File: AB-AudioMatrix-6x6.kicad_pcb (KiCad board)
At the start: 2 copper layers, 204 x 103 mm, 53 parts, among them J1 AudioJack2_Ground_Switch, J10 AudioJack2_Ground_Switch, J11 AudioJack2_Ground_Switch, J12 AudioJack2_Ground_Switch, J13 Conn_01x24, J14 Conn_01x24, J15 Screw_Terminal_01x03, J16 Conn_01x24, J17 Conn_01x24, J2 AudioJack2_Ground_Switch, J3 AudioJack2_Ground_Switch, J4 AudioJack2_Ground_Switch, J5 AudioJack2_Ground_Switch, J6 AudioJack2_Ground_Switch, J7 AudioJack2_Ground_Switch, J8 AudioJack2_Ground_Switch, J9 AudioJack2_Ground_Switch, SW1 SW_Rotary2x6, SW2 SW_Rotary2x6, SW3 SW_Rotary2x6, SW4 SW_Rotary2x6, SW5 SW_Rotary2x6, SW6 SW_Rotary2x6, U1 TL072, U2 TL072, U3 TL072, U4 TL072, U5 TL072, U6 TL072

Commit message: added Edge.Cuts | devices arranged on PCB | added GND planes
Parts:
- added ?: Symbol_CreativeCommonsPublicDomain_SilkScreenTop_Small, Symbol:Symbol_CreativeCommonsPublicDomain_SilkScreenTop_Small, F.Cu at (97.0, 154.9)
- added REF**: KiCad-Logo2_6mm_SilkScreen, Symbol:KiCad-Logo2_6mm_SilkScreen, F.Cu at (51.0, 154.7)
- added REF**: MountingHole_3.2mm_M3, MountingHole:MountingHole_3.2mm_M3, F.Cu at (47.0, 100.0)
- added REF**: MountingHole_3.2mm_M3, MountingHole:MountingHole_3.2mm_M3, F.Cu at (138.0, 100.0)
- added REF**: MountingHole_3.2mm_M3, MountingHole:MountingHole_3.2mm_M3, F.Cu at (148.0, 100.0)
- added REF**: MountingHole_3.2mm_M3, MountingHole:MountingHole_3.2mm_M3, F.Cu at (239.0, 100.0)
- added REF**: MountingHole_3.2mm_M3, MountingHole:MountingHole_3.2mm_M3, F.Cu at (113.0, 110.0)
- added REF**: MountingHole_3.2mm_M3, MountingHole:MountingHole_3.2mm_M3, F.Cu at (173.0, 110.0)
- added REF**: OSHW-Logo2_9.8x8mm_SilkScreen, Symbol:OSHW-Logo2_9.8x8mm_SilkScreen, F.Cu at (64.0, 154.0)
- added REF**: Symbol_CC-Attribution_CopperTop_Small, Symbol:Symbol_CC-Attribution_CopperTop_Small, F.Cu at (72.0, 155.0)
- added REF**: MountingHole_3.2mm_M3, MountingHole:MountingHole_3.2mm_M3, F.Cu at (47.0, 144.0)
- added REF**: MountingHole_3.2mm_M3, MountingHole:MountingHole_3.2mm_M3, F.Cu at (113.0, 144.0)
- added REF**: MountingHole_3.2mm_M3, MountingHole:MountingHole_3.2mm_M3, F.Cu at (173.0, 144.0)
- added REF**: MountingHole_3.2mm_M3, MountingHole:MountingHole_3.2mm_M3, F.Cu at (239.0, 144.0)
- added REF**: MountingHole_3.2mm_M3, MountingHole:MountingHole_3.2mm_M3, F.Cu at (239.0, 110.0)
- added REF**: MountingHole_3.2mm_M3, MountingHole:MountingHole_3.2mm_M3, F.Cu at (47.0, 110.0)
- J1, J10, J11, J12, J2, J3, J4, J5, J6, J7, J8, J9: value AudioJack2_Ground_Switch -> Switchcraft-35RAPC4BH3
- J13, J14, J16, J17, R1, R10, R11, R12, R13, R14, R15, R16, R17, R18, R19, R2, R20, R21, R22, R23, R24, R3, R4, R5, R6, R7, R8, R9, U1, U2, U3, U4, U5, U6: moved to B.Cu
- moved R18 234.1 mm to (230.1, 83.0)
- moved R24 230.7 mm to (237.1, 83.0)
- moved R23 215.0 mm to (221.7, 83.0)
- moved R21 211.4 mm to (190.9, 83.0)
- moved R17 209.7 mm to (214.7, 83.0)
- moved R16 207.2 mm to (199.3, 83.0)
- moved R14 202.5 mm to (168.5, 83.0)
- moved R22 201.0 mm to (206.3, 83.0)
- moved R20 199.7 mm to (175.5, 83.0)
- moved R15 195.7 mm to (183.9, 83.0)
- moved R13 182.3 mm to (153.1, 83.0)
- moved R12 181.8 mm to (129.1, 83.0), turned to 90 degrees
- moved R19 180.1 mm to (160.1, 83.0)
- moved R5 179.3 mm to (120.7, 83.0), turned to 90 degrees
- moved R8 178.3 mm to (67.5, 83.0), turned to 90 degrees
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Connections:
- J15 pad 1: +9V -> -9V
- J15 pad 3: -9V -> +9V
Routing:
- added copper zone on In1.Cu, net GND
- added copper zone on In2.Cu, net GND
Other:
- board size 204 x 103 mm -> 200 x 70 mm
- copper layers 2 -> 4
- board text added: "+"
- board text added: "—"

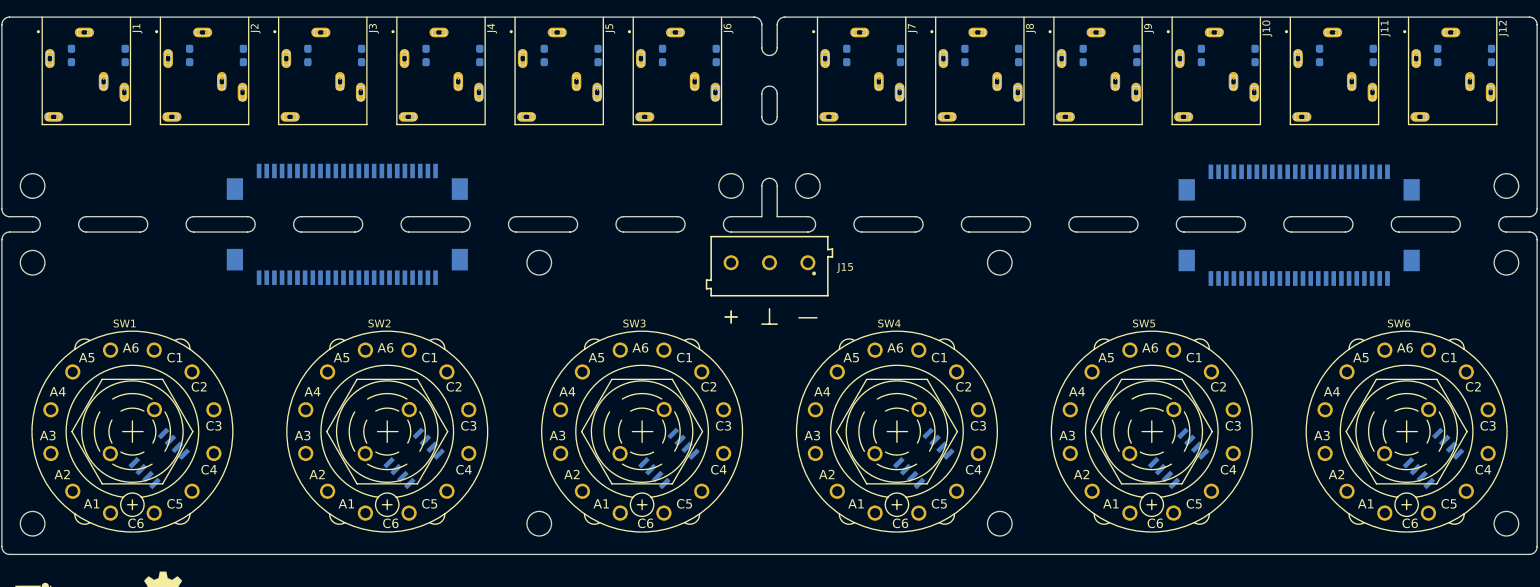
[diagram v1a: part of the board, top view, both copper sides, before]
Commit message: added converter for asymmetric power supply | Routing In & Out PCB finished | Routing Switch PCB started
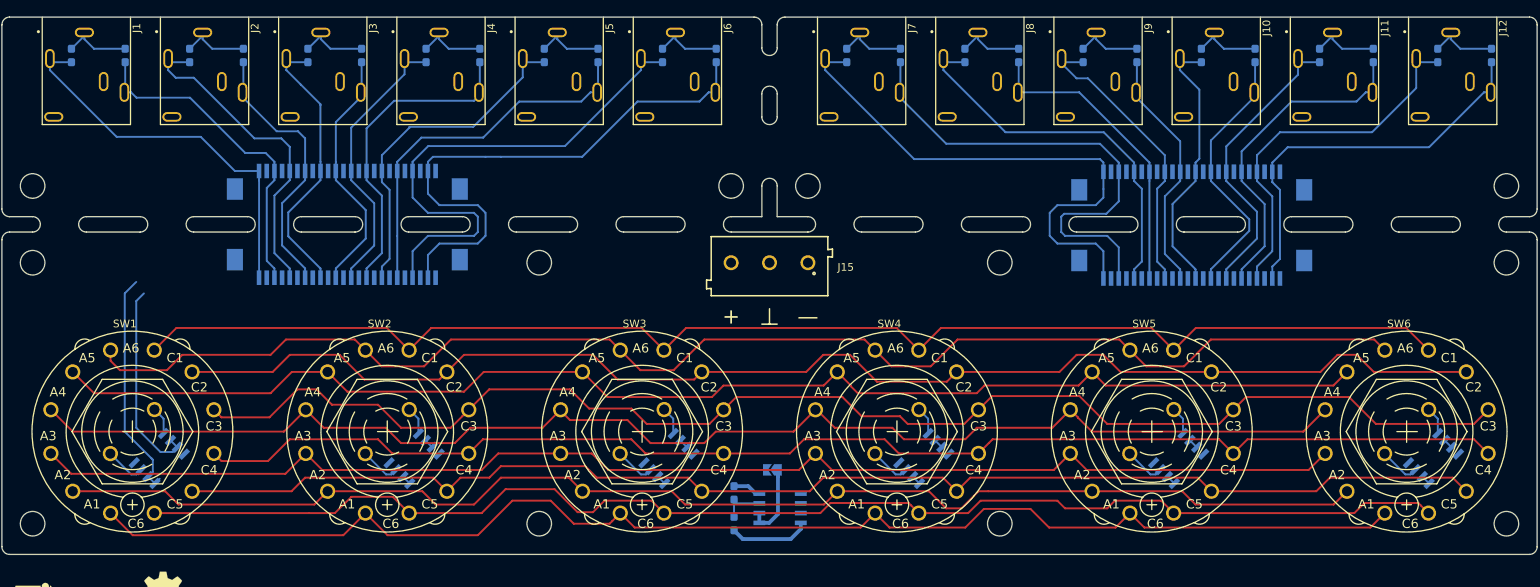
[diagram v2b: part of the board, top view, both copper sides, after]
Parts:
- added JP1: SolderJumper_2_Open, Jumper:SolderJumper-2_P1.3mm_Open_TrianglePad1.0x1.5mm, B.Cu at (143.4, 137.0)
- added R25: 100k, Resistor_SMD:R_0603_1608Metric_Pad1.05x0.95mm_HandSolder, B.Cu at (138.4, 144.0)
- added R26: 100k, Resistor_SMD:R_0603_1608Metric_Pad1.05x0.95mm_HandSolder, B.Cu at (138.4, 140.0)
- added U7: TL072, Package_SO:SOIC-8_3.9x4.9mm_P1.27mm, B.Cu at (144.4, 142.0)
- moved J16 14.0 mm to (198.0, 109.1)
- moved J17 14.0 mm to (198.0, 101.1)
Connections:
- J13 pad 1: In1R -> In1L
- J13 pad 11: In3L -> In3R
- J13 pad 13: In4R -> In4L
- J13 pad 15: In4L -> In4R
- J13 pad 17: In5R -> In5L
- J13 pad 19: In5L -> In5R
- J13 pad 21: In6R -> In6L
- J13 pad 23: In6L -> In6R
- J13 pad 3: In1L -> In1R
- J13 pad 5: In2R -> In2L
- J13 pad 7: In2L -> In2R
- J13 pad 9: In3R -> In3L
- J14 pad 10: In4L -> In4R
- J14 pad 12: In4R -> In4L
- J14 pad 14: In3L -> In3R
- J14 pad 16: In3R -> In3L
- J14 pad 18: In2L -> In2R
- J14 pad 2: In6L -> In6R
- J14 pad 20: In2R -> In2L
- J14 pad 22: In1L -> In1R
- J14 pad 24: In1R -> In1L
- J14 pad 4: In6R -> In6L
- J14 pad 6: In5L -> In5R
- J14 pad 8: In5R -> In5L
- J16 pad 1: Out1R -> Out1L
- J16 pad 11: Out3L -> Out3R
- J16 pad 13: Out4R -> Out4L
- J16 pad 15: Out4L -> Out4R
- J16 pad 17: Out5R -> Out5L
- J16 pad 19: Out5L -> Out5R
- J16 pad 21: Out6R -> Out6L
- J16 pad 23: Out6L -> Out6R
- J16 pad 3: Out1L -> Out1R
- J16 pad 5: Out2R -> Out2L
- J16 pad 7: Out2L -> Out2R
- J16 pad 9: Out3R -> Out3L
- J17 pad 10: Out4L -> Out4R
- J17 pad 12: Out4R -> Out4L
- J17 pad 14: Out3L -> Out3R
- J17 pad 16: Out3R -> Out3L
- J17 pad 18: Out2L -> Out2R
- J17 pad 2: Out6L -> Out6R
- J17 pad 20: Out2R -> Out2L
- J17 pad 22: Out1L -> Out1R
- J17 pad 24: Out1R -> Out1L
- J17 pad 4: Out6R -> Out6L
- J17 pad 6: Out5L -> Out5R
- J17 pad 8: Out5R -> Out5L
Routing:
- net In6L: track 0.00 -> 250.5 mm
- net In6R: track 0.00 -> 248.3 mm
- net In1L: track 0.00 -> 231.1 mm
- net In5R: track 0.00 -> 223.5 mm
- net In5L: track 0.00 -> 221.8 mm
- net In1R: track 0.00 -> 221.1 mm
- net In4L: track 0.00 -> 219.1 mm
- net In2L: track 0.00 -> 218.2 mm
- net In4R: track 0.00 -> 216.4 mm
- net In3R: track 0.00 -> 216.2 mm
- net In2R: track 0.00 -> 213.5 mm
- net In3L: track 0.00 -> 212.2 mm
- net GND: track 0.00 -> 114.4 mm
- net Out1L: track 0.00 -> 102.4 mm
- net Out1R: track 0.00 -> 90.5 mm
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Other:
- net class Default: via_dia 0.8 -> 0.9; via_drill 0.4 -> 0.45
- net class Power added: clearance 0.2, trace_width 0.5, via_dia 0.9, via_drill 0.45

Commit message: Routing switches complete
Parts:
- removed the REF** at (113.0, 110.0)
- removed the REF** at (173.0, 110.0)
- removed the REF** at (113.0, 144.0)
- removed the REF** at (173.0, 144.0)
- added REF**: MountingHole_3.2mm_M3, MountingHole:MountingHole_3.2mm_M3, F.Cu at (176.0, 100.0)
- added REF**: MountingHole_3.2mm_M3, MountingHole:MountingHole_3.2mm_M3, F.Cu at (110.0, 110.0)
- added REF**: MountingHole_3.2mm_M3, MountingHole:MountingHole_3.2mm_M3, F.Cu at (176.0, 110.0)
- added REF**: MountingHole_3.2mm_M3, MountingHole:MountingHole_3.2mm_M3, F.Cu at (110.0, 100.0)
- added REF**: MountingHole_3.2mm_M3, MountingHole:MountingHole_3.2mm_M3, F.Cu at (110.0, 144.0)
- added REF**: MountingHole_3.2mm_M3, MountingHole:MountingHole_3.2mm_M3, F.Cu at (176.0, 144.0)
- moved JP1 1.00 mm to (143.4, 136.0)
- moved R25 1.00 mm to (138.4, 143.0)
- moved R26 1.00 mm to (138.4, 139.0)
- moved SW1 1.00 mm to (60.0, 131.0)
- moved SW2 1.00 mm to (93.2, 131.0)
- moved SW3 1.00 mm to (126.4, 131.0)
- moved SW4 1.00 mm to (159.6, 131.0)
- moved SW5 1.00 mm to (192.8, 131.0)
- moved SW6 1.00 mm to (226.0, 131.0)
- moved U1 1.00 mm to (63.5, 134.5)
- moved U2 1.00 mm to (96.7, 134.5)
- moved U3 1.00 mm to (129.9, 134.5)
- moved U4 1.00 mm to (163.1, 134.5)
- moved U5 1.00 mm to (196.3, 134.5)
- moved U6 1.00 mm to (229.5, 134.5)
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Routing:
- net In6R: track 248.3 -> 256.2 mm
- net In3L: track 212.2 -> 219.5 mm
- net In4R: track 216.4 -> 222.2 mm
- net In2L: track 218.2 -> 223.1 mm
- net In5R: track 223.5 -> 226.2 mm
- net In1L: track 231.1 -> 232.9 mm
- net In4L: track 219.1 -> 217.8 mm
- net In3R: track 216.2 -> 216.7 mm

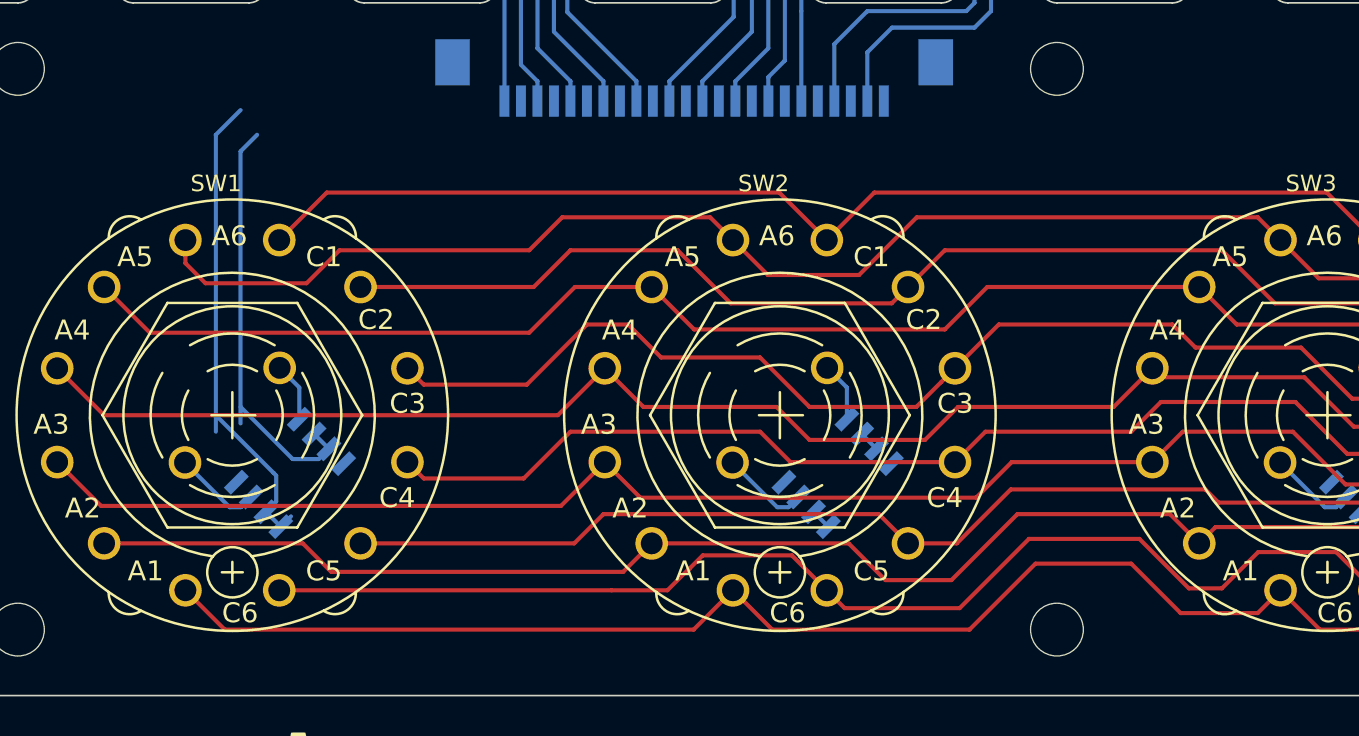
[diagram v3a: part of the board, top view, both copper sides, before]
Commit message: Routing Input FFC connector to switches
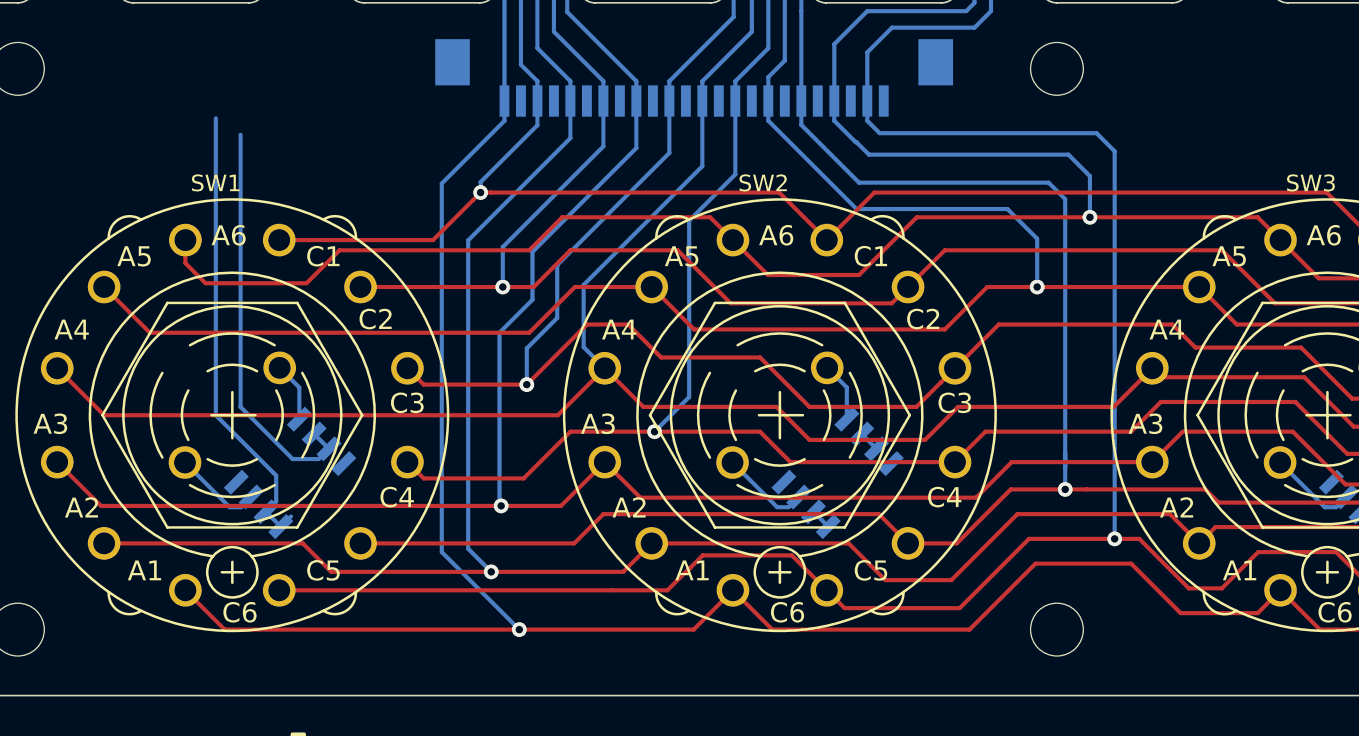
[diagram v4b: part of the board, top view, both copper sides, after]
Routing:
- net In6R: track 256.2 -> 296.7 mm, vias 0 -> 1
- net In5R: track 226.2 -> 264.0 mm, vias 0 -> 1
- net In1L: track 232.9 -> 268.4 mm, vias 0 -> 1
- net In2L: track 223.1 -> 254.8 mm, vias 0 -> 1
- net In3L: track 219.5 -> 247.6 mm, vias 0 -> 1
- net In5L: track 221.3 -> 244.7 mm, vias 0 -> 1
- net In4R: track 222.2 -> 244.3 mm, vias 0 -> 1
- net In3R: track 216.7 -> 237.5 mm, vias 0 -> 1
- net In6L: track 250.3 -> 270.9 mm, vias 0 -> 1
- net In4L: track 217.8 -> 237.6 mm
- net In2R: track 213.5 -> 227.3 mm, vias 0 -> 1
- net In1R: track 221.1 -> 228.1 mm, vias 0 -> 1
- net Out1L: track 102.4 -> 100.3 mm
- net Out1R: track 90.5 -> 89.1 mm

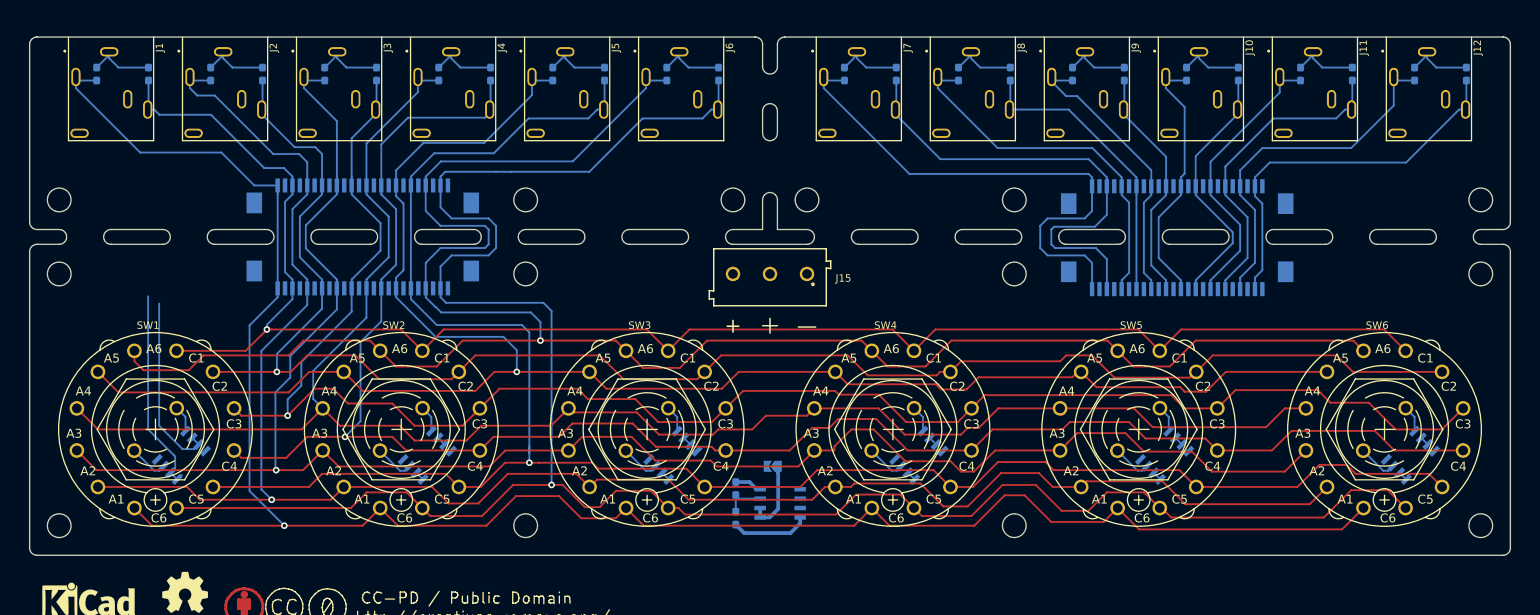
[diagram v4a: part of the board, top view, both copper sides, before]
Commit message: swaped supply pins | routing complete → routing revision and optimization necessary
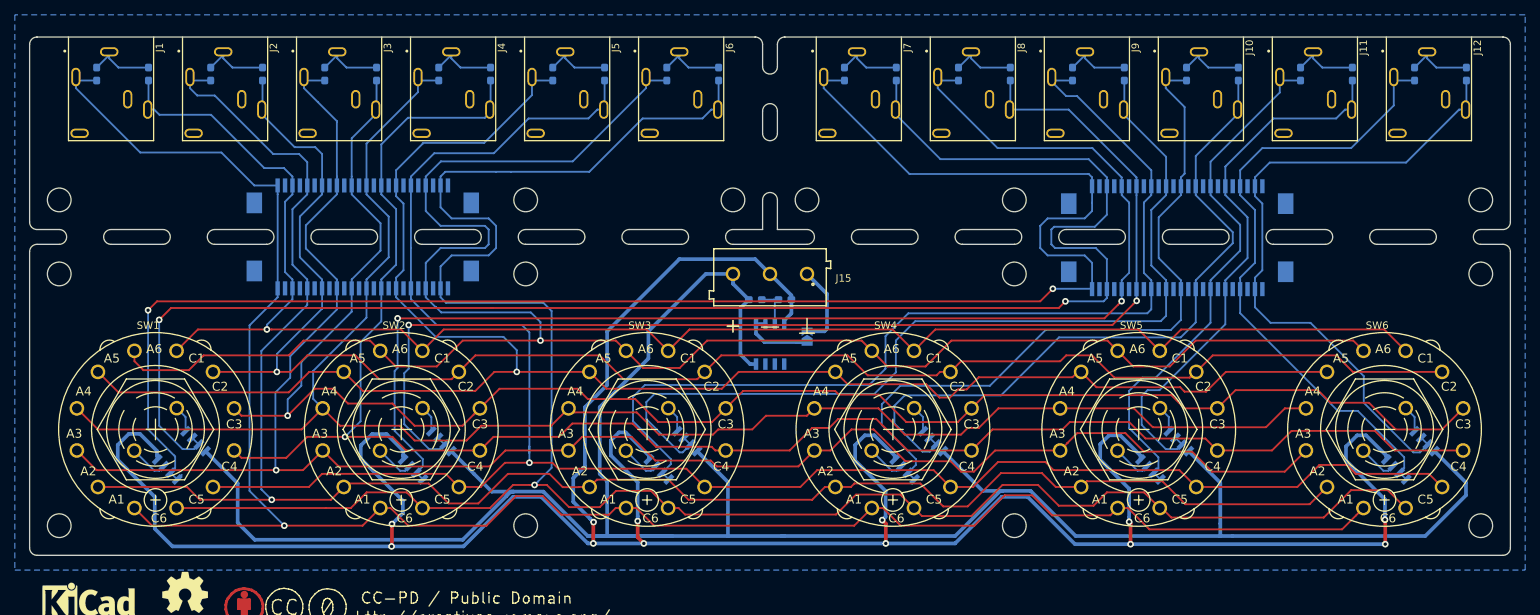
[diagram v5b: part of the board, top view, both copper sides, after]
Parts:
- moved R25 29.6 mm to (141.0, 113.5), turned to 180 degrees
- moved R26 26.4 mm to (145.0, 113.5), turned to 180 degrees
- moved U7 21.6 mm to (143.0, 119.5), turned to 270 degrees
- moved JP1 18.1 mm to (148.0, 118.5), turned to 90 degrees
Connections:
- J15 pad 1: -9V -> GND
- J15 pad 2: GND -> -9V
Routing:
- net -9V: track 3.70 -> 383.3 mm, vias 0 -> 12
- net +9V: track 10.5 -> 317.8 mm
- net Out1R: track 89.1 -> 217.7 mm, vias 0 -> 2
- net Out1L: track 100.3 -> 227.6 mm, vias 0 -> 2
- net Out2L: track 51.6 -> 174.9 mm, vias 0 -> 2
- net Out2R: track 41.3 -> 163.6 mm, vias 0 -> 2
- net Out3L: track 40.2 -> 133.2 mm
- net Out3R: track 33.5 -> 125.2 mm
- net Out4L: track 36.7 -> 97.6 mm
- net Out4R: track 36.0 -> 95.9 mm
- net Out6R: track 53.4 -> 89.9 mm
- net Out6L: track 50.2 -> 86.0 mm
- net Out5L: track 40.1 -> 72.4 mm
- net Out5R: track 44.5 -> 75.5 mm
- net GND: track 114.4 -> 125.7 mm
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- added copper zone on B.Cu, net GND
